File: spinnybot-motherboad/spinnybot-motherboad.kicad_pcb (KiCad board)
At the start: 2 copper layers, 71 parts, among them J1 ENCODER 1, J11 POWER SW2, J12 LEDSTRIP3, J13 LEDSTRIP2, J14 LEDSTRIP3, J2 LEDSTRIP1, J3 LEDSTRIP1, J4 LEDSTRIP2, J5 ENCODER 2, J6 ENCODER 3, J7 SM10B-SRSS-TB, J9 POWER SW1, Q1 SISA96DN, Q2 SISA96DN, Q3 BC846, Q4 Q_NMOS_DGS, U1 LM1117-3.3, U10 MMA3221KEG, U11 ADS122U04IPWR, U12 ADS122U04IPWR, U2 XBP9B-DMWTB002, U3 MC14504BDR2G, U4 ICM-20649, U5 ESP32-DEVKITC-32D, U6 74LVC1G157GV_125, U7 SN74AHCT541DW, U8 SN74LVC1G18DBVR, U9 MMA3221KEG

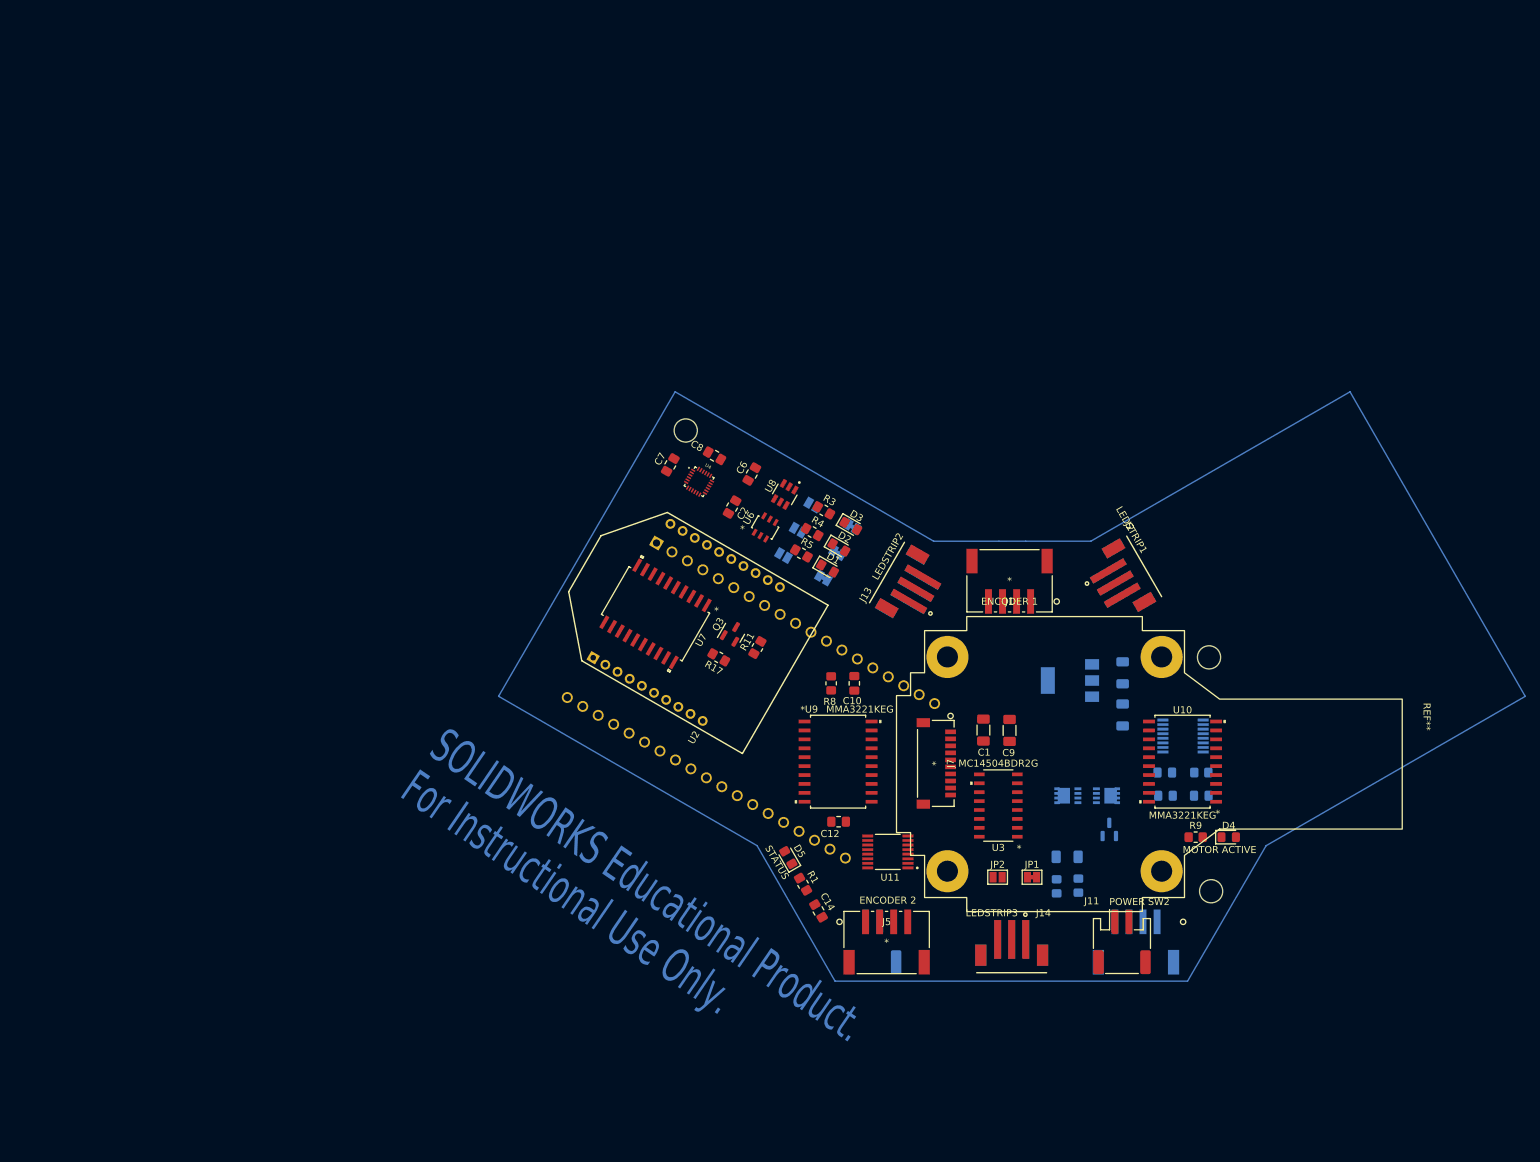
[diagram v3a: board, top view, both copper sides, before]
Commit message: Power pads added, beginning routing
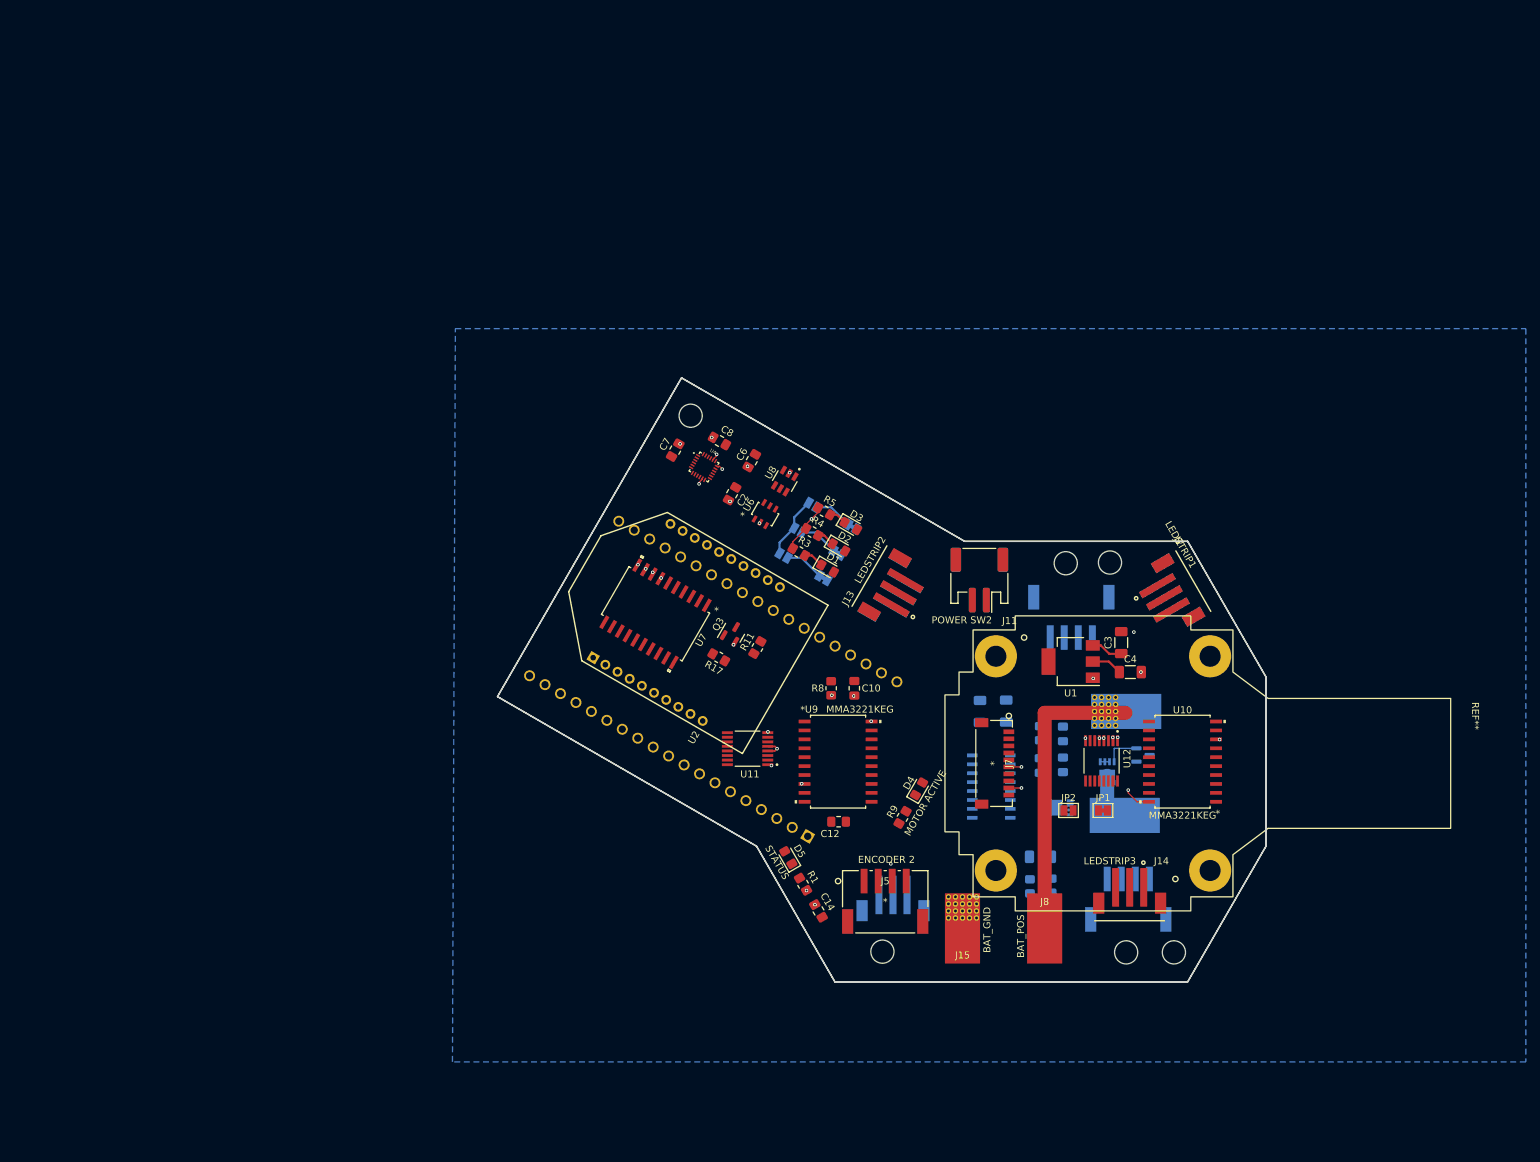
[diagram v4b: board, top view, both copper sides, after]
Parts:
- added H2: STRAINHOLE1, custom:MountingHole_3.3mm, F.Cu at (169.0, 90.5)
- added H5: STRAINHOLE2, custom:MountingHole_3.3mm, F.Cu at (142.9, 145.8)
- added H6: STRAINHOLE3, custom:MountingHole_3.3mm, F.Cu at (177.6, 145.9)
- added J10: ESC_POS, custom:Stitched_SolderWirePad_1x01_SMD_5x10mm, B.Cu at (177.6, 111.6)
- added J15: BAT_GND, custom:Stitched_SolderWirePad_1x01_SMD_5x10mm, F.Cu at (154.3, 142.5)
- added J16: ESC_GND, Connector_Wire:SolderWirePad_1x01_SMD_5x10mm, B.Cu at (177.4, 126.4)
- added J8: BAT_POS, Connector_Wire:SolderWirePad_1x01_SMD_5x10mm, F.Cu at (166.0, 142.5)
- C1, C9, J1, U3: moved to B.Cu
- C3, C4, U1, U12: moved to F.Cu
- moved J11 55.4 mm to (156.7, 92.9), turned to 180 degrees
- moved J9 53.7 mm to (156.7, 92.9), turned to 0 degrees
- moved D4 44.6 mm to (148.1, 122.6), turned to 60 degrees
- moved R9 41.8 mm to (145.8, 126.7), turned to 60 degrees
- moved U11 24.8 mm to (123.7, 116.9)
- moved R2 23.7 mm to (165.3, 114.7), turned to -90 degrees
- moved C15 21.6 mm to (168.6, 114.8), turned to -90 degrees
- moved H4 19.5 mm to (175.3, 90.4)
- moved J14 18.4 mm to (178.1, 138.9)
- moved J12 18.0 mm to (144.4, 140.0)
- moved C13 17.8 mm to (165.3, 119.3), turned to 90 degrees
- moved C11 15.2 mm to (168.6, 119.2), turned to 90 degrees
- moved JP1 13.9 mm to (174.3, 125.7)
- moved JP2 13.9 mm to (169.4, 125.7)
- moved U12 12.1 mm to (174.1, 118.6), turned to -90 degrees
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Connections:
- Q2 pad 5: /ESC_GND -> /Power/ESC_GND
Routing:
- net /Power/ESC_POS: track 0.00 -> 42.3 mm
- net GND: track 0.00 -> 21.9 mm, vias 0 -> 37
- net /Connectors/ESC_S4: track 0.00 -> 8.91 mm
- net /Power/ESC_GND: track 0.00 -> 6.68 mm
- net /ESC_S3: track 0.00 -> 5.61 mm
- net /ESC_S2: track 0.00 -> 5.53 mm
- net /ESC_S1: track 0.00 -> 5.51 mm
- net /POWER_ON: track 0.00 -> 5.05 mm
- net +5V: track 0.00 -> 4.56 mm
- net +3V3: track 0.00 -> 4.41 mm
- net Net-(D1-Pad1): track 0.00 -> 2.89 mm
- net Net-(D2-Pad1): track 0.00 -> 2.55 mm
- net Net-(D3-Pad1): track 0.00 -> 2.50 mm
- added copper zone on B.Cu, net GND
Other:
- board outline added: 109.4 x 86 mm
- rule pad_to_mask_clearance: 0 -> 0.0508
- board text removed: "For Instructional Use Only."
- board text removed: "SOLIDWORKS Educational Product."

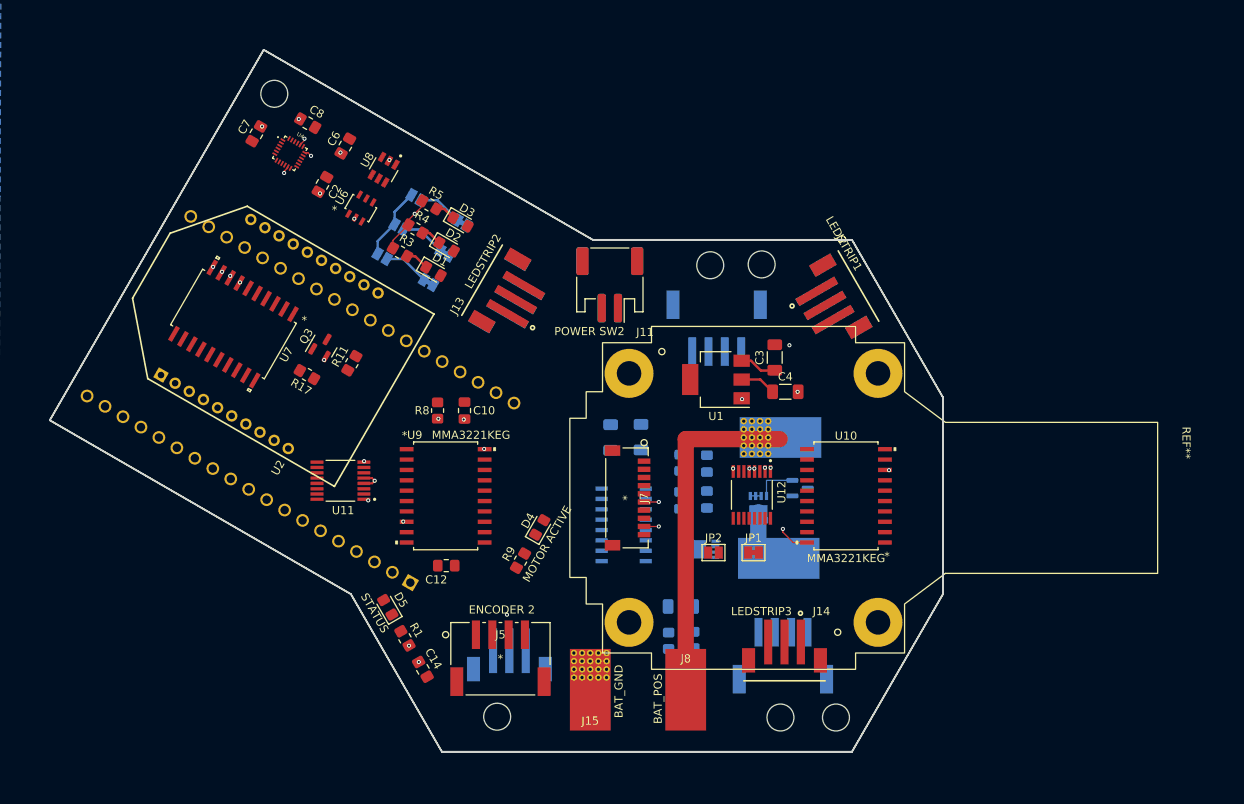
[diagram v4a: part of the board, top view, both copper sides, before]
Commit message: Finishing routing board, needs checking over to make sure everything looks good
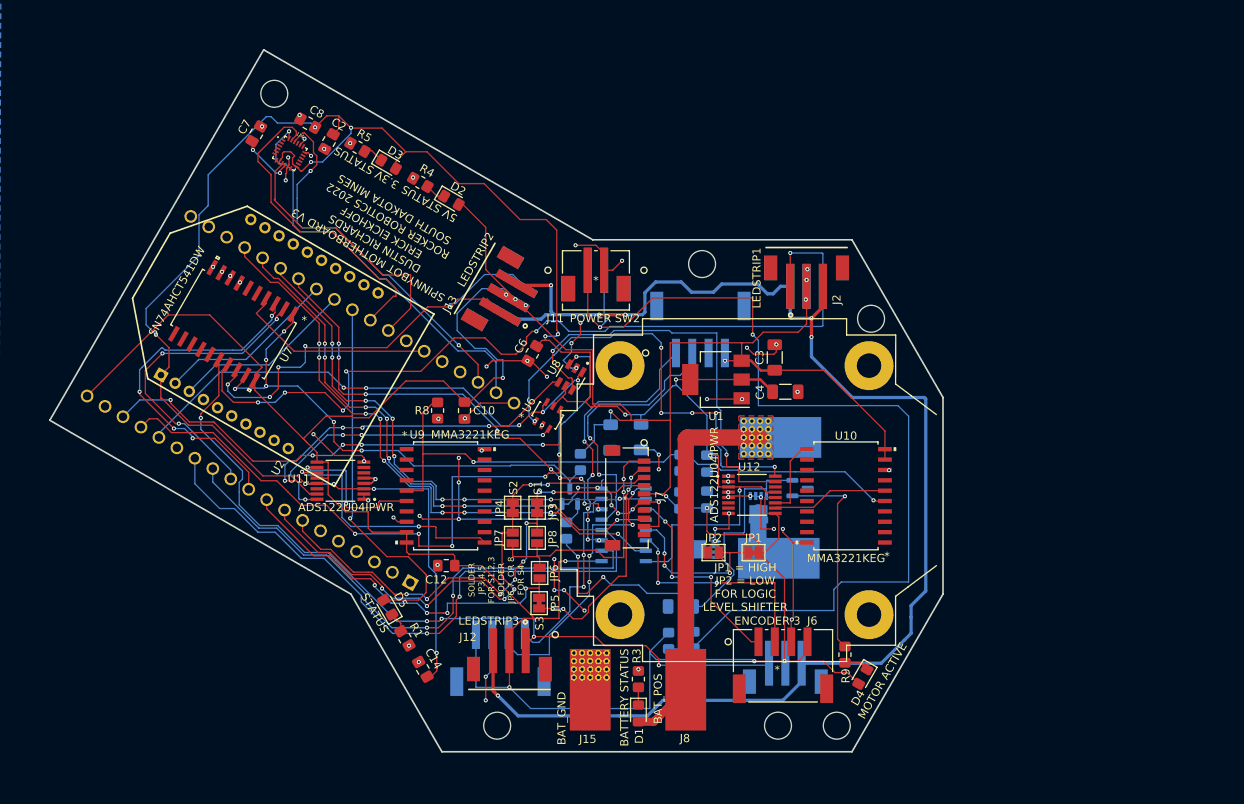
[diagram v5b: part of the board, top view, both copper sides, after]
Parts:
- J11, J9: footprint Connector_JST:JST_PH_S2B-PH-SM4-TB_1x02-1MP_P2.00mm_Horizontal -> B2B-PH-SM4-TB(LF)(SN):B2B-PH-SM4-TBLFSN
- J12, J6, JP3, JP4, JP5, JP6, JP7, JP8: moved to F.Cu
- J14, J5, Q3, R11, R17: moved to B.Cu
- moved R3 59.9 mm to (160.2, 141.2), turned to -90 degrees
- moved D1 59.7 mm to (160.2, 145.4), turned to -90 degrees
- moved JP8 44.2 mm to (147.8, 123.9), turned to 90 degrees
- moved D4 43.6 mm to (187.7, 140.9), turned to -120 degrees
- moved JP6 43.3 mm to (148.1, 128.2), turned to -90 degrees
- moved JP5 41.6 mm to (148.0, 131.9), turned to 90 degrees
- moved R9 41.4 mm to (185.5, 138.2), turned to -90 degrees
- moved JP7 40.6 mm to (144.8, 123.9), turned to 90 degrees
- moved R17 37.1 mm to (151.4, 123.0), turned to -90 degrees
- moved JP3 36.1 mm to (147.8, 120.2), turned to -90 degrees
- moved Q3 35.4 mm to (151.8, 118.8), turned to 90 degrees
- moved U8 34.2 mm to (151.9, 104.2)
- moved U6 34.2 mm to (149.1, 108.9)
- moved C6 34.2 mm to (147.2, 101.3)
- moved JP4 32.3 mm to (144.8, 120.2), turned to -90 degrees
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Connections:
- J10 pad 1: /Power/ESC_POS -> +12V
- J8 pad 1: /Power/ESC_POS -> +12V
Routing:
- net +5V: track 4.56 -> 400.5 mm, vias 0 -> 15
- net +3V3: track 4.41 -> 272.1 mm, vias 0 -> 14
- net /LEDSTRIP_GND: track 0.00 -> 171.5 mm, vias 0 -> 6
- net GND: track 21.9 -> 161.3 mm, vias 37 -> 70
- net Net-(J11-Pad2): track 0.00 -> 122.5 mm, vias 0 -> 2
- net /LEDSTRIP1_DATA_5V: track 0.00 -> 106.3 mm, vias 0 -> 6
- net /LEDSTRIP3_DATA_5V: track 0.00 -> 98.2 mm, vias 0 -> 5
- net /ADC_TX: track 0.00 -> 86.6 mm, vias 0 -> 6
- net /MCU and Buffers/ENC_1B_3V3: track 0.00 -> 74.6 mm, vias 0 -> 2
- net /MCU and Buffers/ENC_3B_3V3: track 0.00 -> 73.8 mm, vias 0 -> 9
- net /ACCEL_SELF_TEST: track 0.00 -> 73.6 mm, vias 0 -> 2
- net /MCU and Buffers/ENC_3A_3V3: track 0.00 -> 70.4 mm, vias 0 -> 9
- net /MCU and Buffers/ENC_1A_3V3: track 0.00 -> 67.7 mm, vias 0 -> 2
- net /MCU and Buffers/ENC_2B_3V3: track 0.00 -> 65.4 mm, vias 0 -> 9
- net /ADC_SEL: track 0.00 -> 62.7 mm, vias 0 -> 5
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- added copper zone on F.Cu, net +12V
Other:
- board text added: "3.3V STATUS"
- board text added: "5V STATUS"
- board text added: "BATTERY STATUS"
- board text added: "ESC GND"
- board text added: "ESC POS"
- board text added: "JP1 = HIGH JP2 = LOW FOR LOGIC LEVEL SHIFTER"
- board text added: "S1"
- board text added: "S2"
- board text added: "S3"
- board text added: "SOLDER JP3,4,5 FOR S1,2,3 SOLDER JP6,7, OR 8 FOR S4"
- board text added: "SPIN SPIN SPIN SPIN SPIN SPIN SPIN SPIN SPIN SPIN SPIN SPIN SPIN SPIN SPIN SPIN SPIN SPIN SPIN SPIN SPIN SPIN SPIN SPIN SPIN SPIN SPIN SPIN SPIN SPIN SPIN SPIN SPIN SPIN SPIN SPIN SPIN SPIN SPIN SPIN SPIN SPIN SPIN SPIN SPIN SPIN SPIN SPIN SPIN SPIN SPIN SPIN SPIN SPIN SPIN SPIN SPIN SPIN SPIN SPIN SPIN SPIN SPIN SPIN SPIN SPIN SPIN SPIN SPIN SPIN SPIN SPIN SPIN SPIN SPIN SPIN SPIN SPIN SPIN SPIN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"
- board text added: "SPINNYBOT MOTHERBOARD V3 DUSTIN RICHARDS ERICK EICKHOFF ROCKER ROBOTICS 2022 SOUTH DAKOTA MINES"

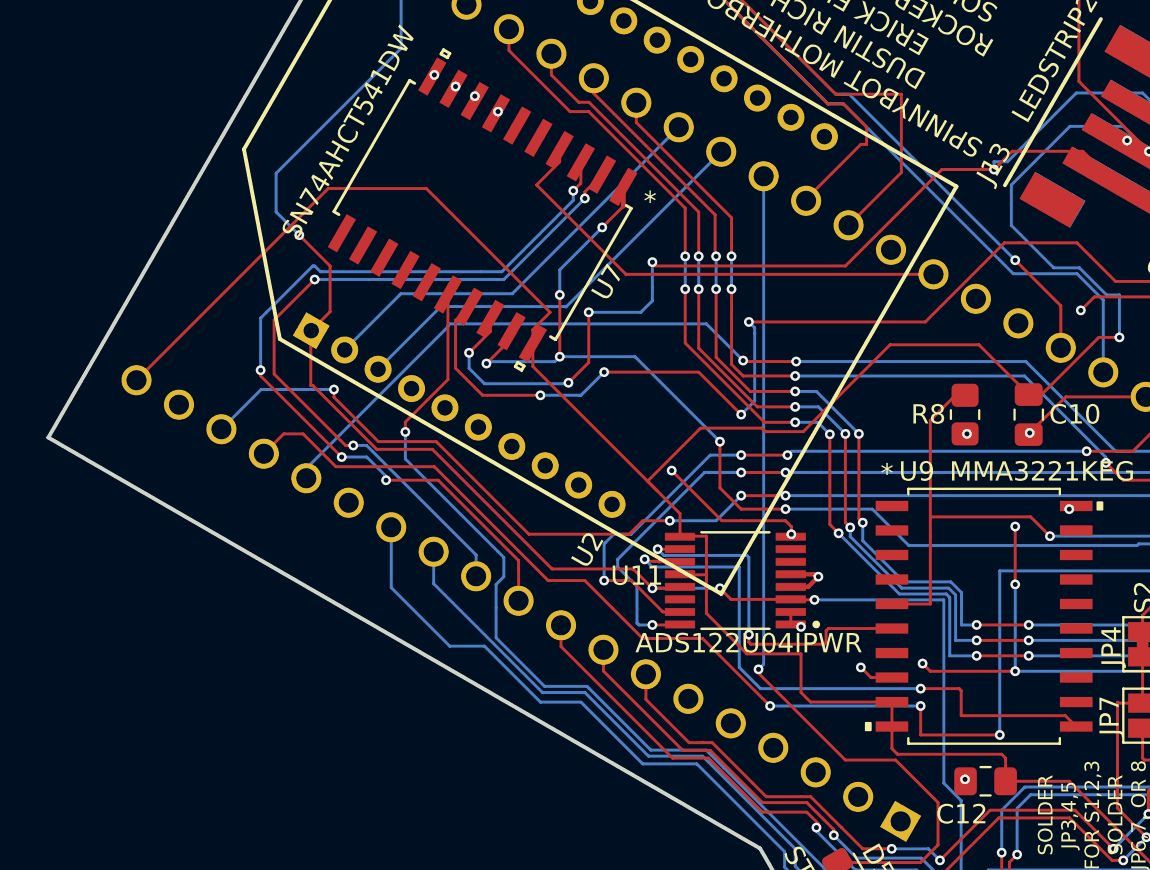
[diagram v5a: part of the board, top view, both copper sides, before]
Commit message: Added chip names and solder jumper instructions
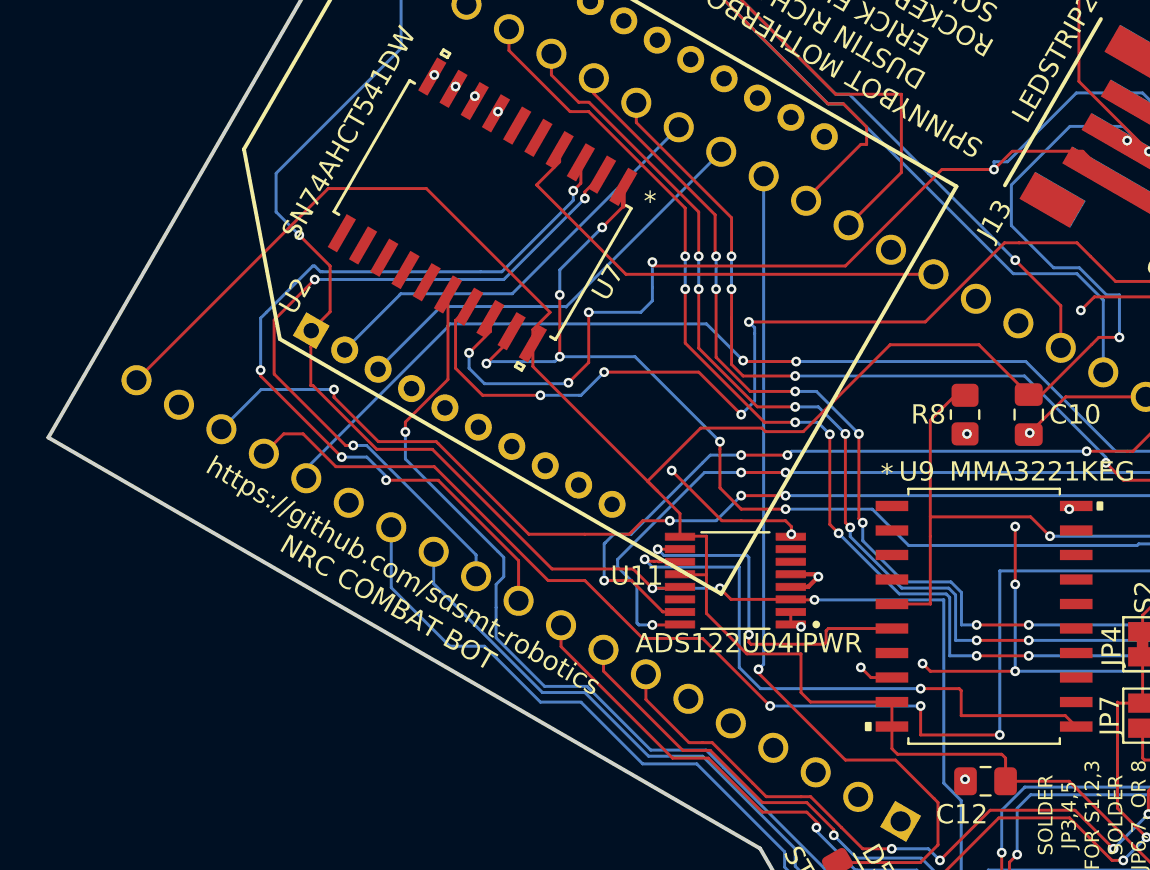
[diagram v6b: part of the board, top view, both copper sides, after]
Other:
- board text added: "https://github.com/sdsmt-robotics NRC COMBAT BOT"
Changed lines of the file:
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@@
     (property "Sheetname" "MCU and Buffers")
     (attr through_hole)
-    (fp_text reference "U2" (at -13.664375 9.345125 60) (layer "F.SilkS")
+    (fp_text reference "U2" (at -9.855515 -10.360253 60) (layer "F.SilkS")
       (effects (font (size 1.002165 1.002165) (thickness 0.15)))
     )
@@
     (property "Sheetname" "Connectors")
     (attr through_hole)
-    (fp_text reference "J13" (at -5.325 -3.55 60) (layer "F.SilkS")
+    (fp_text reference "J13" (at -7.875575 -2.054999 60) (layer "F.SilkS")
       (effects (font (size 1.001866 1.001866) (thickness 0.15)) (justify left))
     )
@@
     (effects (font (size 1 1) (thickness 0.15)))
   )
+  (gr_text "https://github.com/sdsmt-robotics\nNRC COMBAT BOT" (at 106.1 117.355 330) (layer "F.SilkS")
+    (effects (font (size 1 1) (thickness 0.15)))
+  )
